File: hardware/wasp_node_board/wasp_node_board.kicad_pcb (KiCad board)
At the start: 4 copper layers, 115 parts, among them J1 Conn_01x02, J2 RJ45_Hanrun_HR911105A_Horizon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, J3 Conn_02x10_Odd_Even, J4 RJ45_Hanrun_HR911105A_Horizon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, J5 RJ45_Hanrun_HR911105A_Horizon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, J6 TC2030, J7 USB_C_Receptacle_USB2.0_16P, SW1 C&K JS102011SAQN, SW2 C&K KMR231NG LFS, U1 STM32H723ZGTx, U2 USBLC6-2SC6, U3 APS6404L-3SQRx-SN, U4 TPSM863253RDXR, U5 KSZ8794CNXCC, U6 LP5907MFX-1.2, Y1 TSX-3225 25.00M-N0YYYYG30RGB, Y2 ASE-25.000MHZ-L-K-T

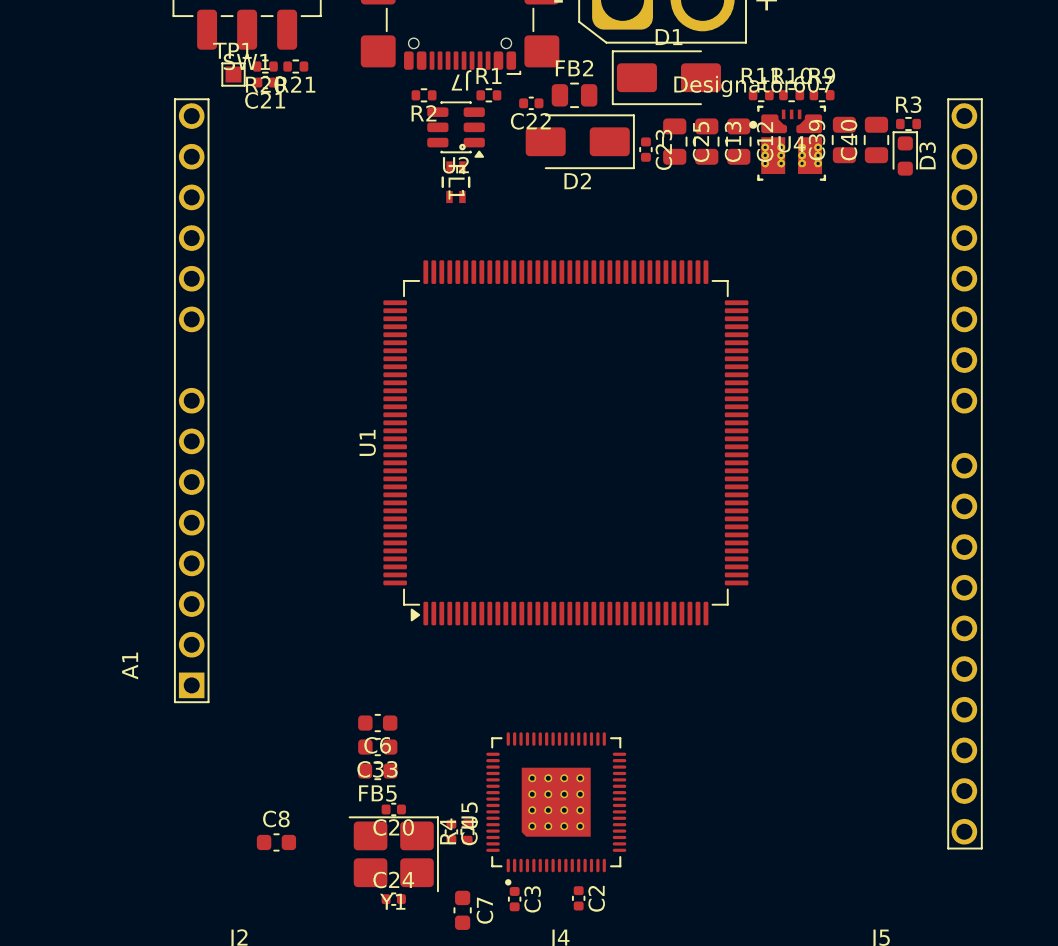
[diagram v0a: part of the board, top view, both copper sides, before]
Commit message: Board setup for OSH Park — FR408 stackup, impedance net classes, DRC rules
Co-Authored-By: Claude Opus 5 <noreply@anthropic.com>
Claude-Session: https://claude.ai/code/session_01R5uaLk4w44r9dBy8LCo6if
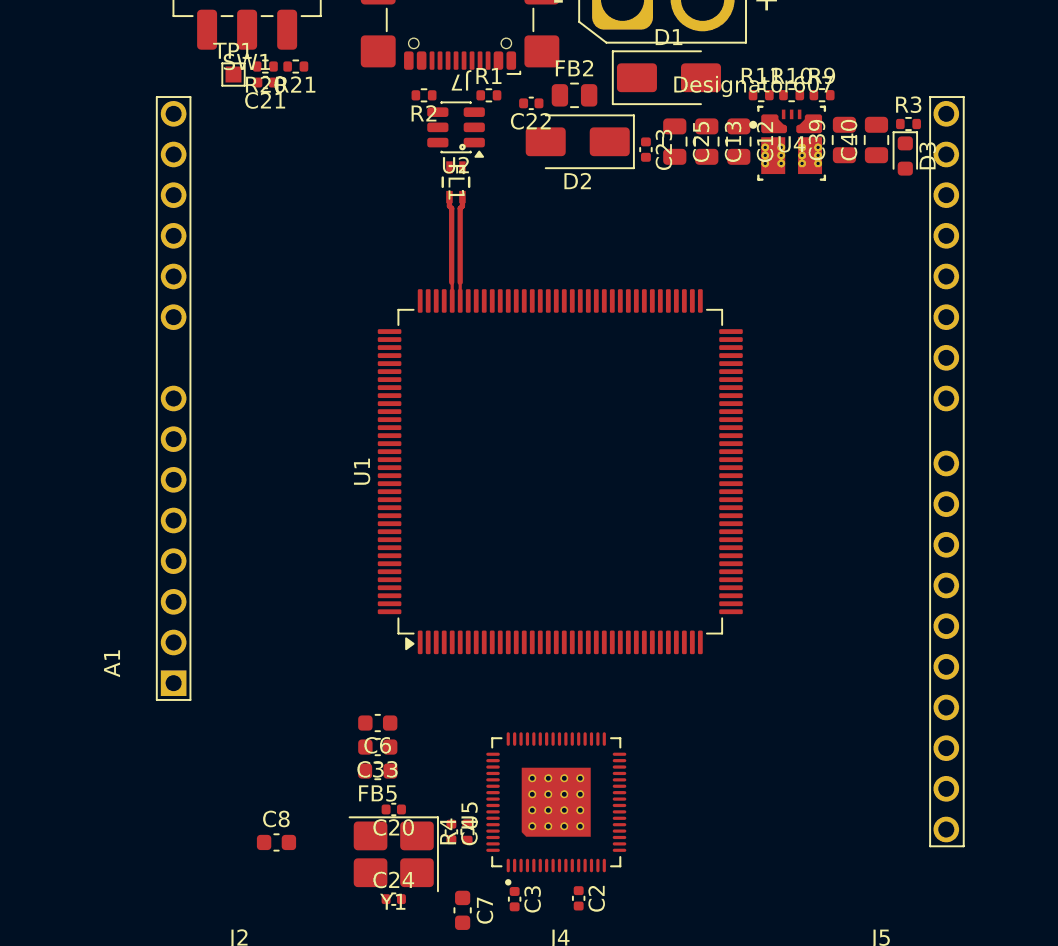
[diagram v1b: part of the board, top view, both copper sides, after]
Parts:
- moved U1 1.83 mm to (211.7, 110.3)
- moved A1 1.14 mm to (187.5, 123.5)
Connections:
- net /ethernet/RX1_n renamed /ethernet/RX1_N
- net /ethernet/RX1_p renamed /ethernet/RX1_P
- net /ethernet/TX1_n renamed /ethernet/TX1_N
- net /ethernet/TX1_p renamed /ethernet/TX1_P
- net Net-(J4-RD+) renamed /ethernet/TX2_P
- net Net-(J4-RD-) renamed /ethernet/TX2_N
- net Net-(J4-TD+) renamed /ethernet/RX2_P
- net Net-(J4-TD-) renamed /ethernet/RX2_N
- net Net-(J5-RD+) renamed /ethernet/TX3_P
- net Net-(J5-RD-) renamed /ethernet/TX3_N
- net Net-(J5-TD+) renamed /ethernet/RX3_P
- net Net-(J5-TD-) renamed /ethernet/RX3_N
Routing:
- net USB_D_P: track 0.00 -> 6.56 mm
- net USB_D_N: track 0.00 -> 6.55 mm
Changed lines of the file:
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@@
 	(generator_version "9.0")
 	(general
-		(thickness 1.6)
+		(thickness 1.5622)
 		(legacy_teardrops no)
 	)
@@
 			(layer "F.Mask"
 				(type "Top Solder Mask")
-				(thickness 0.01)
+				(thickness 0.0254)
 			)
 			(layer "F.Cu"
 				(type "copper")
-				(thickness 0.035)
+				(thickness 0.0432)
 			)
 			(layer "dielectric 1"
 				(type "prepreg")
-				(thickness 0.1)
-				(material "FR4")
-				(epsilon_r 4.5)
-				(loss_tangent 0.02)
+				(thickness 0.1999)
+				(material "FR408HG 2113")
+				(epsilon_r 3.7)
+				(loss_tangent 0.0092)
 			)
 			(layer "In1.Cu"
 				(type "copper")
-				(thickness 0.035)
+				(thickness 0.0173)
 			)
 			(layer "dielectric 2"
-				(type "core")
-				(thickness 1.24)
-				(material "FR4")
-				(epsilon_r 4.5)
-				(loss_tangent 0.02)
+				(type "prepreg")
+				(thickness 0.9906)
+				(material "FR408HR")
+				(epsilon_r 3.7)
+				(loss_tangent 0.0092)
 			)
 			(layer "In2.Cu"
 				(type "copper")
-				(thickness 0.035)
+				(thickness 0.0173)
 			)
 			(layer "dielectric 3"
 				(type "prepreg")
-				(thickness 0.1)
-				(material "FR4")
-				(epsilon_r 4.5)
-				(loss_tangent 0.02)
+				(thickness 0.1999)
+				(material "FR408HG 2113")
+				(epsilon_r 3.7)
+				(loss_tangent 0.0092)
 			)
 			(layer "B.Cu"
 				(type "copper")
-				(thickness 0.035)
+				(thickness 0.0432)
 			)
 			(layer "B.Mask"
 				(type "Bottom Solder Mask")
-				(thickness 0.01)
+				(thickness 0.0254)
 			)
 			(layer "B.Paste"
@@
 				(type "Bottom Silk Screen")
 			)
-			(copper_finish "None")
+			(copper_finish "ENIG")
 			(dielectric_constraints no)
 		)
@@
 	(net 51 "USB_D_P")
 	(net 52 "/power/USB_EMI_D_P")
-	(net 53 "/ethernet/TX1_p")
+	(net 53 "/ethernet/TX1_P")
 	(net 54 "Net-(J2-Pad11)")
 	(net 55 "Net-(J2-Pad10)")
-	(net 56 "/ethernet/RX1_p")
+	(net 56 "/ethernet/RX1_P")
 	(net 57 "unconnected-(J2-NC-Pad7)")
 	(net 58 "Net-(J2-Pad12)")
-	(net 59 "/ethernet/RX1_n")
+	(net 59 "/ethernet/RX1_N")
 	(net 60 "Net-(J2-Pad9)")
-	(net 61 "/ethernet/TX1_n")
+	(net 61 "/ethernet/TX1_N")
 	(net 62 "/mcu/USART3_RX")
 	(net 63 "/mcu/SPI2_SCK")
@@
 	(net 76 "/mcu/SPI2_MISO")
 	(net 77 "/mcu/PA8")
-	(net 78 "Net-(J4-RD-)")
-	(net 79 "Net-(J4-RD+)")
-	(net 80 "Net-(J4-TD-)")
+	(net 78 "/ethernet/TX2_N")
+	(net 79 "/ethernet/TX2_P")
+	(net 80 "/ethernet/RX2_N")
 	(net 81 "Net-(J4-Pad10)")
 	(net 82 "Net-(J4-Pad12)")
 	(net 83 "Net-(J4-Pad9)")
 	(net 84 "Net-(J4-Pad11)")
-	(net 85 "Net-(J4-TD+)")
+	(net 85 "/ethernet/RX2_P")
 	(net 86 "unconnected-(J4-NC-Pad7)")
-	(net 87 "Net-(J5-RD-)")
+	(net 87 "/ethernet/TX3_N")
 	(net 88 "Net-(J5-Pad12)")
 	(net 89 "Net-(J5-Pad10)")
 	(net 90 "Net-(J5-Pad11)")
-	(net 91 "Net-(J5-TD+)")
-	(net 92 "Net-(J5-TD-)")
+	(net 91 "/ethernet/RX3_P")
+	(net 92 "/ethernet/RX3_N")
 	(net 93 "Net-(J5-Pad9)")
 	(net 94 "unconnected-(J5-NC-Pad7)")
-	(net 95 "Net-(J5-RD+)")
+	(net 95 "/ethernet/TX3_P")
 	(net 96 "/mcu/SWO{slash}TDO")
 	(net 97 "/mcu/SWCLK{slash}TCK")
@@
 			(remove_unused_layers no)
 			(roundrect_rratio 0.167)
-			(net 91 "Net-(J5-TD+)")
+			(net 91 "/ethernet/RX3_P")
 			(pinfunction "TD+")
 			(pintype "passive")
@@
 			(layers "*.Cu" "*.Mask")
 			(remove_unused_layers no)
-			(net 92 "Net-(J5-TD-)")
+			(net 92 "/ethernet/RX3_N")
 			(pinfunction "TD-")
 			(pintype "passive")
@@
 			(layers "*.Cu" "*.Mask")
 			(remove_unused_layers no)
-			(net 95 "Net-(J5-RD+)")
+			(net 95 "/ethernet/TX3_P")
 			(pinfunction "RD+")
 			(pintype "passive")
@@
 			(layers "*.Cu" "*.Mask")
 			(remove_unused_layers no)
-			(net 87 "Net-(J5-RD-)")
+			(net 87 "/ethernet/TX3_N")
 			(pinfunction "RD-")
 			(pintype "passive")
@@
 	(footprint "Arduino_UNO_R3_Headers:Arduino_UNO_R3_Headers"
 		(layer "F.Cu")
-		(at 188.63 123.65 90)
+		(at 187.5 123.51 90)
 		(descr "Arduino UNO R3 shield headers only - board outline and full-board courtyard removed, per-header courtyards added")
 		(tags "Arduino UNO R3")
@@
 			(size 0.85 0.2)
 			(layers "F.Cu" "F.Mask" "F.Paste")
-			(net 56 "/ethernet/RX1_p")
+			(net 56 "/ethernet/RX1_P")
 			(pinfunction "RXP1")
 			(pintype "input")
@@
 			(size 0.85 0.2)
 			(layers "F.Cu" "F.Mask" "F.Paste")
-			(net 59 "/ethernet/RX1_n")
+			(net 59 "/ethernet/RX1_N")
 			(pinfunction "RXM1")
 			(pintype "input")
@@
 			(size 0.85 0.2)
 			(layers "F.Cu" "F.Mask" "F.Paste")
-			(net 53 "/ethernet/TX1_p")
+			(net 53 "/ethernet/TX1_P")
 			(pinfunction "TXP1")
 			(pintype "output")
@@
 			(size 0.85 0.2)
 			(layers "F.Cu" "F.Mask" "F.Paste")
-			(net 61 "/ethernet/TX1_n")
+			(net 61 "/ethernet/TX1_N")
 			(pinfunction "TXM1")
 			(pintype "output")
@@
 			(size 0.85 0.2)
 			(layers "F.Cu" "F.Mask" "F.Paste")
-			(net 85 "Net-(J4-TD+)")
+			(net 85 "/ethernet/RX2_P")
 			(pinfunction "RXP2")
 			(pintype "input")
@@
 			(size 0.85 0.2)
 			(layers "F.Cu" "F.Mask" "F.Paste")
-			(net 80 "Net-(J4-TD-)")
+			(net 80 "/ethernet/RX2_N")
 			(pinfunction "RXM2")
 			(pintype "input")
@@
 			(size 0.85 0.2)
 			(layers "F.Cu" "F.Mask" "F.Paste")
-			(net 79 "Net-(J4-RD+)")
+			(net 79 "/ethernet/TX2_P")
 			(pinfunction "TXP2")
 			(pintype "output")
@@
 			(size 0.85 0.2)
 			(layers "F.Cu" "F.Mask" "F.Paste")
-			(net 78 "Net-(J4-RD-)")
+			(net 78 "/ethernet/TX2_N")
 			(pinfunction "TXM2")
 			(pintype "output")
@@
 			(size 0.85 0.2)
 			(layers "F.Cu" "F.Mask" "F.Paste")
-			(net 91 "Net-(J5-TD+)")
+			(net 91 "/ethernet/RX3_P")
 			(pinfunction "RXP3")
 			(pintype "input")
@@
 			(size 0.85 0.2)
 			(layers "F.Cu" "F.Mask" "F.Paste")
-			(net 92 "Net-(J5-TD-)")
+			(net 92 "/ethernet/RX3_N")
 			(pinfunction "RXM3")
 			(pintype "input")
@@
 			(size 0.85 0.2)
 			(layers "F.Cu" "F.Mask" "F.Paste")
-			(net 95 "Net-(J5-RD+)")
+			(net 95 "/ethernet/TX3_P")
 			(pinfunction "TXP3")
 			(pintype "output")
@@
 			(size 0.85 0.2)
 			(layers "F.Cu" "F.Mask" "F.Paste")
-			(net 87 "Net-(J5-RD-)")
+			(net 87 "/ethernet/TX3_N")
 			(pinfunction "TXM3")
 			(pintype "output")
@@
 			(remove_unused_layers no)
 			(roundrect_rratio 0.167)
-			(net 85 "Net-(J4-TD+)")
+			(net 85 "/ethernet/RX2_P")
 			(pinfunction "TD+")
 			(pintype "passive")
@@
 			(layers "*.Cu" "*.Mask")
 			(remove_unused_layers no)
-			(net 80 "Net-(J4-TD-)")
+			(net 80 "/ethernet/RX2_N")
 			(pinfunction "TD-")
 			(pintype "passive")
@@
 			(layers "*.Cu" "*.Mask")
 			(remove_unused_layers no)
-			(net 79 "Net-(J4-RD+)")
+			(net 79 "/ethernet/TX2_P")
 			(pinfunction "RD+")
 			(pintype "passive")
@@
 			(layers "*.Cu" "*.Mask")
 			(remove_unused_layers no)
-			(net 78 "Net-(J4-RD-)")
+			(net 78 "/ethernet/TX2_N")
 			(pinfunction "RD-")
 			(pintype "passive")
@@
 	(footprint "Package_QFP:LQFP-144_20x20mm_P0.5mm"
 		(layer "F.Cu")
-		(at 212 108.5 90)
+		(at 211.65 110.3 90)
 		(descr "LQFP, 144 Pin (JEDEC MS-026 variation BFB, 1.40mm body thickness, https://www.jedec.org/document_search?search_api_views_fulltext=MS-026, https://ww1.microchip.com/downloads/en/PackagingSpec/00000049BQ.pdf#page=425), generated with kicad-footprint-generator ipc_gullwing_generator.py")
 		(tags "LQFP QFP Microchip_144-Lead-Plastic-Low-Profile-Quad-Flatpack-(PL) Microsemi_TQ144")
@@
 			(remove_unused_layers no)
 			(roundrect_rratio 0.167)
-			(net 56 "/ethernet/RX1_p")
+			(net 56 "/ethernet/RX1_P")
 			(pinfunction "TD+")
 			(pintype "passive")
@@
 			(layers "*.Cu" "*.Mask")
 			(remove_unused_layers no)
-			(net 59 "/ethernet/RX1_n")
+			(net 59 "/ethernet/RX1_N")
 			(pinfunction "TD-")
 			(pintype "passive")
@@
 			(layers "*.Cu" "*.Mask")
 			(remove_unused_layers no)
-			(net 53 "/ethernet/TX1_p")
+			(net 53 "/ethernet/TX1_P")
 			(pinfunction "RD+")
 			(pintype "passive")
@@
 			(layers "*.Cu" "*.Mask")
 			(remove_unused_layers no)
-			(net 61 "/ethernet/TX1_n")
+			(net 61 "/ethernet/TX1_N")
 			(pinfunction "RD-")
 			(pintype "passive")
@@
 		)
 	)
+	(segment
+		(start 205.54 93.716499)
+		(end 205.3986 93.857899)
+		(width 0.33)
+		(layer "F.Cu")
+		(net 49)
+	)
+	(segment
+		(start 205.4 99.6375)
+		(end 205.4 98.477801)
+		(width 0.2)
+		(layer "F.Cu")
+		(net 49)
+	)
+	(segment
+		(start 205.4 98.477801)
+		(end 205.3986 98.476401)
+		(width 0.2)
+		(layer "F.Cu")
+		(net 49)
+	)
+	(segment
+		(start 205.3986 93.857899)
+		(end 205.3986 98.476401)
+		(width 0.33)
+		(layer "F.Cu")
+		(net 49)
+	)
+	(segment
+		(start 205.54 93.144998)
+		(end 205.54 93.716499)
+		(width 0.33)
+		(layer "F.Cu")
+		(net 49)
+	)
+	(segment
+		(start 204.7272 93.144998)
+		(end 204.7272 93.716499)
+		(width 0.33)
+		(layer "F.Cu")
+		(net 51)
+	)
+	(segment
+		(start 204.7272 93.716499)
+		(end 204.8686 93.857899)
+		(width 0.33)
+		(layer "F.Cu")
+		(net 51)
+	)
+	(segment
+		(start 204.9 99.6375)
+		(end 204.9 98.507801)
+		(width 0.2)
+		(layer "F.Cu")
+		(net 51)
+	)
+	(segment
+		(start 204.9 98.507801)
+		(end 204.8686 98.476401)
+		(width 0.2)
+		(layer "F.Cu")
+		(net 51)
+	)
+	(segment
+		(start 204.8686 93.857899)
+		(end 204.8686 98.476401)
+		(width 0.33)
+		(layer "F.Cu")
+		(net 51)
+	)
+	(group ""
+		(members "2f0a99ec-6271-4312-9196-df79a752bb80" "79105e99-055c-4dbe-8c3e-71422b5f2edd")
+	)
 	(embedded_fonts no)
